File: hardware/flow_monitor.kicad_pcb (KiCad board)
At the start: 2 copper layers, 60.3 x 44.9 mm, 94 parts, among them J1 Conn_01x07_Pin, J2 USB_C_Receptacle_USB2.0_16P, J3 Conn_01x02_Socket, J4 Conn_01x02_Socket, J5 Conn_01x02_Socket_TOP, J6 Conn_01x02_Socket, J7 Conn_01x02_Socket_BOT, J8 Conn_01x06_Socket, Q1 2N7002, Q2 IRLML6402, Q3 BC807, Q4 BC817, Q5 2N7002, Q6 2N7002, SW1 1TS005F-2500-5001, SW2 1TS005F-2500-5001, SW3 1TS005F-2500-5001, SW4 1TS005F-2500-5001, SW5 SW_SPDT, U1 USBLC6-2SC6, U2 BQ25185DLHR, U3 CH340C, U4 TPS631000, U5 LMV331, U6 STM32G030C8Tx, U7 EA_DOGS164W-A, Y1 Crystal

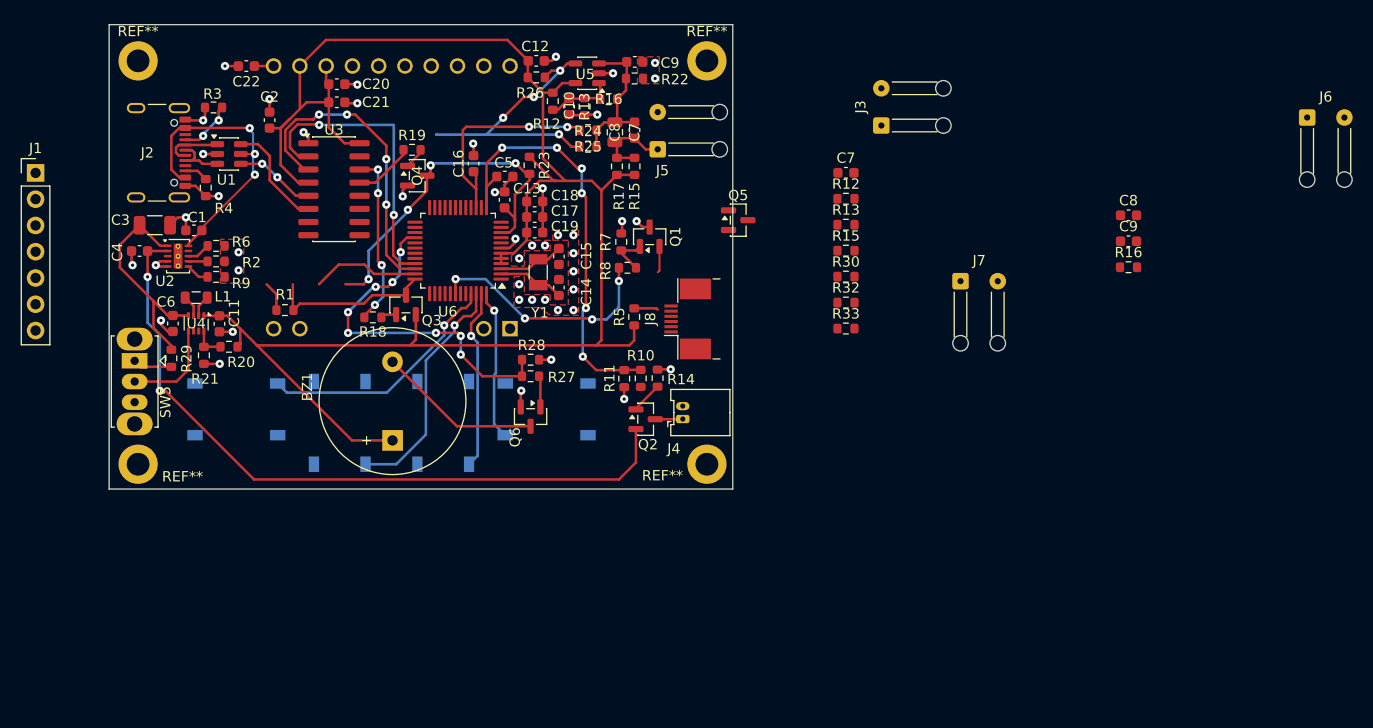
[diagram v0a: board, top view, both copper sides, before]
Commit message: Add Rev-B hardware and firmware baseline
  - InfusionBA2: new STM32G071 project for Rev-B (dual photodiode, LPTIM1 Phase 2)
  - KiCad: Rev-B schematic + PCB (DOGS164, G071, TPS610981, COMP1 simplification)
  - Gerbers + STEP files from JLCPCB order W2026040304309275
  - Logo footprints (ETH, GHE) and generation script
  - Remove stale KiCad backup zips and lock files
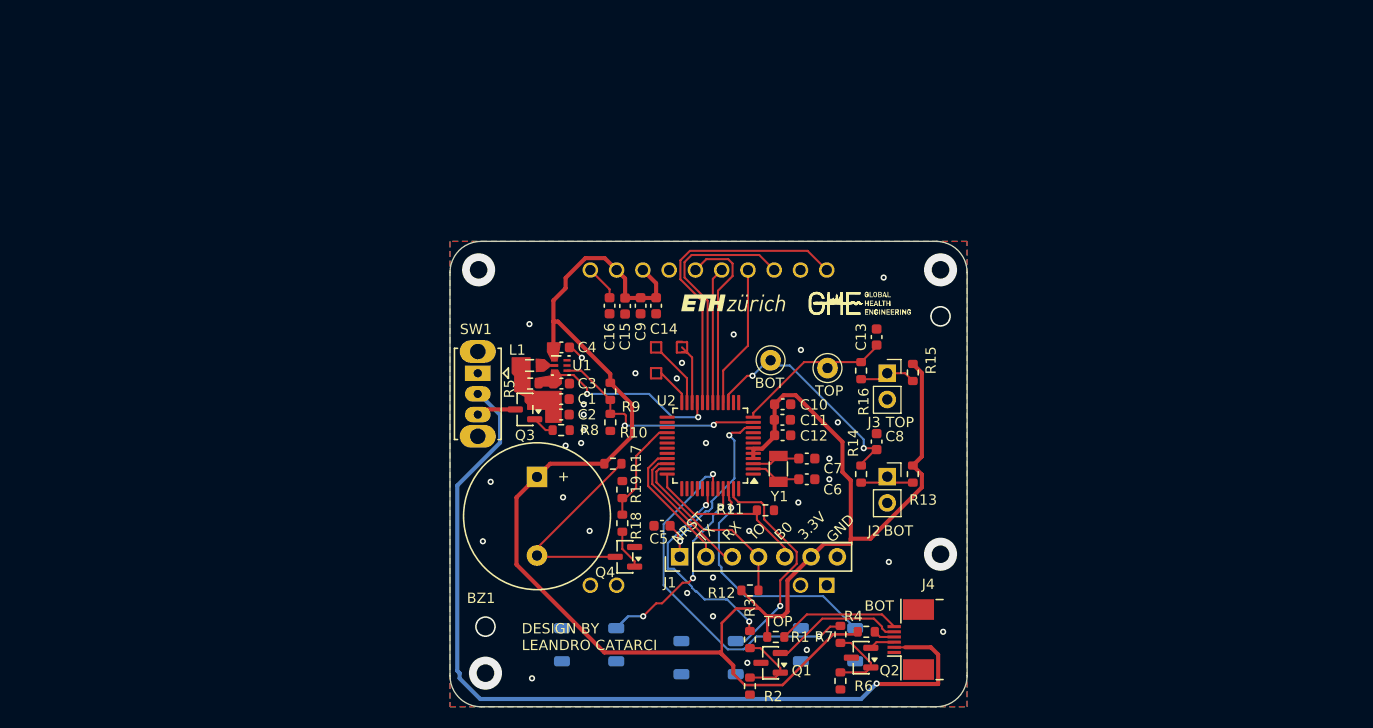
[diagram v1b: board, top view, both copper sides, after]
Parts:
- removed C17, C19: 0.1uF, Capacitor_SMD:C_0603_1608Metric
- removed C18: 1uF, Capacitor_SMD:C_0603_1608Metric
- removed C20: 100nF, Capacitor_SMD:C_0603_1608Metric
- removed C21: 4700nF, Capacitor_SMD:C_0603_1608Metric
- removed C22: 1000nF, Capacitor_SMD:C_0603_1608Metric
- removed the C5 at (146.9, 86.5)
- removed the C7 at (179.9, 86.1)
- removed the C8 at (207.2, 90.2)
- removed the C9 at (207.2, 92.7)
- removed J5: Conn_01x02_Socket_TOP, Connector_Wire:SolderWire-0.1sqmm_1x02_P3.6mm_D0.4mm_OD1mm_Relief
- removed J6: Conn_01x02_Socket, Connector_Wire:SolderWire-0.1sqmm_1x02_P3.6mm_D0.4mm_OD1mm_Relief
- removed J7: Conn_01x02_Socket_BOT, Connector_Wire:SolderWire-0.1sqmm_1x02_P3.6mm_D0.4mm_OD1mm_Relief
- removed J8: Conn_01x06_Socket, Connector_FFC-FPC:Jushuo_AFC07-S06FCA-00_1x6-1MP_P0.50_Horizontal
- removed Q5, Q6: 2N7002, Package_TO_SOT_SMD:SOT-23
- removed the R10 at (160.0, 106.0)
- removed the R11 at (158.4, 106.0)
- removed the R12 at (179.9, 88.6)
- removed the R13 at (179.9, 91.1)
- removed the R13 at (154.6, 79.7)
- removed the R14 at (161.6, 106.0)
- removed the R15 at (179.9, 93.7)
- removed the R16 at (207.2, 95.2)
- removed R20: 511kΩ, Resistor_SMD:R_0603_1608Metric
- removed R21: 91kΩ, Resistor_SMD:R_0603_1608Metric
- removed R22: 1MΩ, Resistor_SMD:R_0603_1608Metric
- removed R23, R26, R28, R29: 10kΩ, Resistor_SMD:R_0603_1608Metric
- removed R24, R27, R33: 100Ω, Resistor_SMD:R_0603_1608Metric
- removed R25: 330kΩ, Resistor_SMD:R_0603_1608Metric
- removed R30: 1800Ω, Resistor_SMD:R_0603_1608Metric
- removed R32: 100kΩ, Resistor_SMD:R_0603_1608Metric
- removed REF** (x4): MountingHole_2.2mm_M2_DIN965_Pad, MountingHole:MountingHole_2.2mm_M2_DIN965_Pad
- removed SW2, SW3, SW4: 1TS005F-2500-5001, IV_Flow_Monitor_Footprints:SW_HYP_1TS005F-2500-5001
- removed SW5: SW_SPDT, IV_Flow_Monitor_Footprints:X_SW_Slide_SPDT_SSK12D07VG5
- removed U4: TPS631000, Package_TO_SOT_SMD:SOT-583-8
- removed U5: LMV331, Package_TO_SOT_SMD:SOT-23-5
- removed U6: STM32G030C8Tx, Package_QFP:LQFP-48_7x7mm_P0.5mm
- removed U7: EA_DOGS164W-A, Display:EA_DOGS104X-A
- added BOT: TestPoint, TestPoint:TestPoint_Keystone_5000-5004_Miniature, F.Cu at (172.6, 104.2)
- added C4: 22uF, Capacitor_SMD:C_0603_1608Metric, F.Cu at (152.3, 103.0)
- added R13: 3.3kΩ, Resistor_SMD:R_0603_1608Metric, F.Cu at (186.3, 115.2)
- added R17: 1800Ω, Resistor_SMD:R_0603_1608Metric, F.Cu at (157.3, 114.2)
- added R8: 100k, Resistor_SMD:R_0603_1608Metric, F.Cu at (152.3, 111.0)
- added R9: 100k, Resistor_SMD:R_0603_1608Metric, F.Cu at (157.1, 107.2)
- added S1: PTS647SN38SMTR2_LFS, Button_Switch_SMD:SW_SPST_PTS647_Sx38, B.Cu at (178.1, 131.8)
- added S2: PTS647SN38SMTR2_LFS, Button_Switch_SMD:SW_SPST_PTS647_Sx38, B.Cu at (166.6, 133.0)
- added S3: PTS647SN38SMTR2_LFS, Button_Switch_SMD:SW_SPST_PTS647_Sx38, B.Cu at (155.0, 131.8)
- added TP1: TestPoint, TestPoint:TestPoint_Keystone_5000-5004_Miniature, F.Cu at (178.1, 105.0)
- C1: renamed from C2; value 100nF -> 10uF
- C10, C12, C9: value 100nF -> 0.1uF
- C11: value 22uF -> 1uF
- C13: value 0.1mF -> 100pF
- C14: value 20pF -> 100nF
- C15: value 20pF -> 4700nF
- C16: value 100pF -> 1000nF
- C2: renamed from C3; value 10uF -> 100nF; footprint Capacitor_SMD:C_1206_3216Metric -> Capacitor_SMD:C_0603_1608Metric
- C3: renamed from C4; value 1uF -> 100nF
- C5: renamed from C1; value 1uF -> 100nF
- C6: value 22uF -> 20pF
- C7: value 100nF -> 20pF
- C8: value 4700nF -> 100pF; footprint Capacitor_SMD:C_0805_2012Metric -> Capacitor_SMD:C_0603_1608Metric
- J2: value USB_C_Receptacle_USB2.0_16P -> Conn_01x02_Socket_TOP; footprint IV_Flow_Monitor_Footprints:USB_C_Receptacle_GCT_USB4105-xx-A_16P_TopMnt_Horizontal -> Connector_PinSocket_2.54mm:PinSocket_1x02_P2.54mm_Vertical
- J3: value Conn_01x02_Socket -> Conn_01x02_Socket_BOT; footprint Connector_Wire:SolderWire-0.1sqmm_1x02_P3.6mm_D0.4mm_OD1mm_Relief -> Connector_PinSocket_2.54mm:PinSocket_1x02_P2.54mm_Vertical
- J4: value Conn_01x02_Socket -> Conn_01x06_Socket; footprint Connector_Molex:Molex_PicoBlade_53048-0210_1x02_P1.25mm_Horizontal -> Connector_FFC-FPC:Jushuo_AFC07-S06FCA-00_1x6-1MP_P0.50_Horizontal
- L1: value 1uL -> 4.7uH
- Q2: value IRLML6402 -> 2N7002
- Q3: value BC807 -> AO3401A
- Q4: value BC817 -> 2N7002
- R1, R18: value 10kΩ -> 100Ω
- R10: renamed from R12; value 47kΩ -> 100k
- R11: renamed from R2; value 18kΩ -> 10kΩ
- R12: renamed from R3; value 5.1kΩ -> 10kΩ
- R14: renamed from R15; value 10kΩ -> 100Ω
- R15: renamed from R16; value 1MΩ -> 3.3kΩ
- R16: renamed from R17; value 3.3kΩ -> 100Ω
- R2: renamed from R4; value 5.1kΩ -> 100kΩ
- R4: renamed from R6; value 1kΩ -> 100Ω
- R5: renamed from R8; value 100Ω -> 390Ohm
- R7: renamed from R9; value 10kΩ -> 100Ω
- SW1: value 1TS005F-2500-5001 -> SK12D07VG5; footprint IV_Flow_Monitor_Footprints:SW_HYP_1TS005F-2500-5001 -> IV_Flow_Monitor_Footprints:X_SW_Slide_SPDT_SSK12D07VG5; moved to F.Cu
- U1: value USBLC6-2SC6 -> TPS610981DSET; footprint Package_TO_SOT_SMD:SOT-23-6 -> TPS61098DSET:DSE0006A
- U2: value BQ25185DLHR -> STM32G071C8Tx; footprint Package_SON:WSON-10-1EP_2x3mm_P0.5mm_EP0.84x2.4mm_ThermalVias -> Package_QFP:LQFP-48_7x7mm_P0.5mm
- U3: value CH340C -> EA_DOGS164W-A; footprint Package_SO:SOIC-16_3.9x9.9mm_P1.27mm -> IV_Flow_Monitor_Footprints:EA_DOGS164X-A; moved to B.Cu
- moved J2 78.1 mm to (183.8, 115.5), turned to 0 degrees
- moved R4 73.1 mm to (181.8, 130.5), turned to 0 degrees
- moved J1 72.5 mm to (163.8, 123.2), turned to 90 degrees
- moved R2 71.4 mm to (170.6, 135.8), turned to 90 degrees
- moved R12 69.8 mm to (170.6, 126.5)
- moved R7 69.6 mm to (179.3, 130.8), turned to 90 degrees
- moved C6 63.1 mm to (176.1, 115.8), turned to 180 degrees
- moved U3 61.1 mm to (178.0, 126.0), turned to 90 degrees
- moved R11 58.3 mm to (172.1, 118.8), turned to 0 degrees
- moved R1 57.0 mm to (173.1, 131.0), turned to 0 degrees
- moved C11 55.2 mm to (173.7, 110.0), turned to 180 degrees
- moved U2 54.6 mm to (166.7, 112.5), turned to 180 degrees
- moved C5 53.5 mm to (162.1, 120.2), turned to 180 degrees
- moved R6 47.4 mm to (179.3, 135.2), turned to 90 degrees
- moved C2 43.3 mm to (152.3, 109.5)
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- renumbered R5 to R3, R7 to R6
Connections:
- BZ1 pad 2: Net-(BZ1--) -> BZ_DRN
- C1 pad 1: +3.3V -> VBAT_PROT
- C10 pad 1: GND -> +3.3V
- C10 pad 2: /VREF = 1.65V -> GND
- C13 pad 2: NRST -> ADC_IR_DETECTOR_TOP
- C14 pad 1: GND -> +3.3V
- C14 pad 2: /OSC32_IN -> GND
- C15 pad 2: /OSC32_OUT -> +3.3V
- C16 pad 2: ADC_IR_DETECTOR_TOP -> /LCD_VOUT
- C2 pad 2: Net-(U2-SYS) -> VBAT_PROT
- C3 pad 2: Net-(Q2-S) -> ADC_V_BAT
- C5 pad 1: GND -> NRST
- C5 pad 2: +5V -> GND
- C6 pad 2: Net-(U2-SYS) -> /OSC32_IN
- C7 pad 1: /PD_AC -> GND
- C7 pad 2: /PD_K -> /OSC32_OUT
- C8 pad 1: /PD_AC -> GND
- C8 pad 2: /PD_K -> ADC_IR_DETECTOR_BOT
- C9 pad 1: GND -> +3.3V
- C9 pad 2: /PD_AC -> GND
- J1 pad 2: SWDIO -> UART1_TX
- J1 pad 3: BOOT0 -> UART1_RX
- J1 pad 4: UART1_TX -> SWDIO
- J1 pad 5: UART1_RX -> BOOT0
- J3 pad 1: /IR_LED+ -> PD_BIAS_TOP
- J3 pad 2: /IR_LED- -> GND
- J4 pad 1: BAT+ -> GND
- J4 pad 2: BAT- -> BAT+
- L1 pad 1: Net-(U4-LX1) -> VBAT_PROT
- L1 pad 2: Net-(U4-LX2) -> BST_SW
- Q1 pad 1: /LED_GATE_BOT -> /LED_GATE_TOP
- Q1 pad 2: IR_LED_BOT- -> IR_LED_TOP-
- Q2 pad 1: Net-(Q2-G) -> /LED_GATE_BOT
- Q2 pad 2: Net-(Q2-S) -> IR_LED_BOT-
- Q2 pad 3: BAT+ -> GND
- Q3 pad 1: Net-(Q3-B) -> RPOL_GATE
- Q3 pad 2: +3.3V -> VBAT_PROT
- Q3 pad 3: BOOT0 -> VBAT_SW
- Q4 pad 1: Net-(Q4-B) -> /BUZZER_GATE
- Q4 pad 3: NRST -> BZ_DRN
- R1 pad 1: BOOT0 -> +3.3V
- R1 pad 2: GND -> IR_LED_TOP+
- R10 pad 1: +3.3V -> BST_MODE
- R10 pad 2: /VREF = 1.65V -> GND
- R11 pad 1: GND -> BOOT0
- R11 pad 2: Net-(U2-ILIM/VSET) -> GND
- R12 pad 1: GND -> +3.3V
- R12 pad 2: Net-(J2-CC1) -> SWDIO
- R14 pad 1: +3.3V -> ADC_IR_DETECTOR_BOT
- R14 pad 2: /PD_K -> PD_BIAS_BOT
- R15 pad 1: /PD_AC -> +3.3V
- R15 pad 2: /VREF = 1.65V -> PD_BIAS_TOP
- R16 pad 1: +3.3V -> ADC_IR_DETECTOR_TOP
- R16 pad 2: Net-(J5-Pin_1) -> PD_BIAS_TOP
- R18 pad 1: Net-(Q3-B) -> /BUZZER_GATE
- R18 pad 2: UART_RTS -> BUZZER_CTRL
- R19 pad 1: UART_DTR -> GND
- R19 pad 2: Net-(Q4-B) -> BUZZER_CTRL
- R2 pad 1: Net-(J2-CC2) -> GND
- R2 pad 2: GND -> /LED_GATE_TOP
- R3 pad 1: +3.3V -> /LED_GATE_TOP
- R3 pad 2: IR_LED_BOT+ -> LED_CTRL_TOP
- R4 pad 1: GND -> +3.3V
- R4 pad 2: Net-(U2-ISET) -> IR_LED_BOT+
- R5 pad 1: /LED_GATE_BOT -> VBAT_PROT
- R5 pad 2: LED_CTRL_BOT -> ADC_V_BAT
- R7 pad 1: GND -> /LED_GATE_BOT
- R7 pad 2: Net-(U2-TS/MR) -> LED_CTRL_BOT
- SW1 pad 1: BTN_MINUS -> unconnected-(SW1-A-Pad1)
- SW1 pad 2: GND -> BAT+
- SW1 pad 3: unconnected-(SW1-K-Pad3) -> VBAT_SW
- U1 pad 1: Net-(J2-D--PadA7) -> +3.3V
- U1 pad 2: GND -> BST_SW
- U1 pad 3: Net-(J2-D+-PadA6) -> ADC_V_BAT
- U1 pad 4: USB_D+ -> BST_MODE
- U1 pad 5: +5V -> unconnected-(U1-VSUB-Pad5)
- U1 pad 6: USB_D- -> GND
- U2 pad 1: Net-(U2-SYS) -> unconnected-(U2-PC13-Pad1)
- U2 pad 10: +5V -> NRST
- U2 pad 11: unconnected-(U2-VSS-Pad11) -> BST_MODE
- U2 pad 2: Net-(Q2-S) -> /OSC32_IN
- U2 pad 3: unconnected-(U2-STAT2-Pad3) -> /OSC32_OUT
- U2 pad 4: GND -> +3.3V
- U2 pad 5: GND -> +3.3V
- U2 pad 6: Net-(U2-TS/MR) -> +3.3V
- U2 pad 7: Net-(U2-ILIM/VSET) -> GND
- U2 pad 8: Net-(U2-ISET) -> unconnected-(U2-PF0-Pad8)
- U3 pad 1: GND -> unconnected-(U3-NC-Pad1)
- U3 pad 11: unconnected-(U3-~{RI}-Pad11) -> /LCD_VOUT
- U3 pad 12: unconnected-(U3-~{DCD}-Pad12) -> +3.3V
- U3 pad 13: UART_DTR -> +3.3V
- U3 pad 14: UART_RTS -> GND
- U3 pad 15: unconnected-(U3-R232-Pad15) -> LCD_MISO
- U3 pad 16: +3.3V -> LCD_MOSI
- U3 pad 2: UART1_TX -> unconnected-(U3-NC-Pad2)
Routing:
- net BAT+: track 2.66 -> 85.4 mm, vias 0 -> 1
- net Net-(Q2-S): track 69.5 -> 0.00 mm, vias 2 -> 0
- net GND: track 53.7 -> 1.61 mm, vias 46 -> 37
- net (no net): track 44.5 -> 0.00 mm, vias 6 -> 0
- net LED_CTRL_BOT: track 0.00 -> 35.1 mm, vias 0 -> 2
- net LCD_RST: track 0.00 -> 29.9 mm
- net +5V: track 28.4 -> 0.00 mm, vias 3 -> 0
- net DROP_INT: track 27.6 -> 0.00 mm, vias 4 -> 0
- net ADC_V_BAT: track 43.0 -> 18.1 mm, vias 6 -> 2
- net BUZZER_CTRL: track 34.4 -> 10.2 mm, vias 8 -> 0
- net LCD_CS: track 0.00 -> 24.1 mm
- net Net-(U2-SYS): track 22.4 -> 0.00 mm
- net ADC_IR_DETECTOR_BOT: track 0.00 -> 22.4 mm, vias 0 -> 2
- net BST_MODE: track 0.00 -> 21.9 mm, vias 0 -> 2
- net BTN_RES: track 0.00 -> 21.5 mm, vias 0 -> 1
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- added copper zone on B.Cu, net GND
- added copper zone on F.Cu, net MCU_RES1
- added copper zone on F.Cu, net MCU_RES2
- added copper zone on F.Cu, net MCU_RES3
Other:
- board size 60.3 x 44.9 mm -> 50 x 45 mm
- board text added: "3.3V"
- board text added: "B0"
- board text added: "BOT"
- board text added: "DESIGN BY LEANDRO CATARCI"
- board text added: "DRIPITO v2"
- board text added: "GND"
- board text added: "IO"
- board text added: "NRST"
- board text added: "RX"
- board text added: "TOP"
- board text added: "TX"
